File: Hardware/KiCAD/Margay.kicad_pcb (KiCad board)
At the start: 2 copper layers, 50.1 x 30.4 mm, 82 parts, among them J1 SDMMCWR-CRD, J3 CONN_6SCREW_2.54, Q1 DMG3404, Q2 FDN360P, Q3 2N7002, U1 ATMEGA1284M, U10 TLV3691DPF, U11 MIC94090C6, U12 BME280, U13 MAX6070AAUT18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

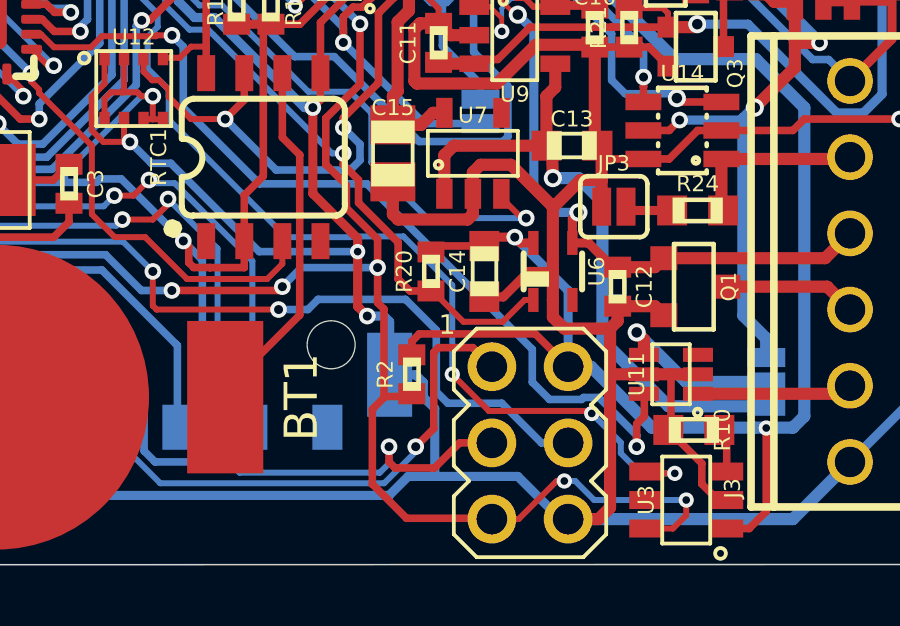
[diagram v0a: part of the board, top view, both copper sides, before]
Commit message: 3V3 --> Schottky diode --> VCoin+. Provide a backup option for the clock if its battery fails: the main batteries of the data logger. Ideally, this would have been connected to VBat to keep the coin cell as just a backup. But I cannot see how to route that trace. However, this will at least serve to protect timekeeping.
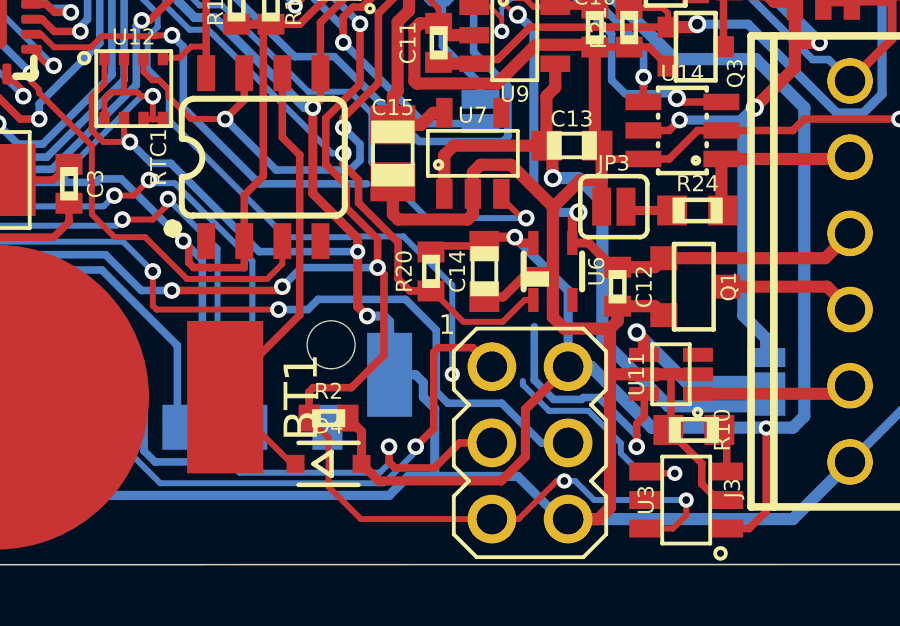
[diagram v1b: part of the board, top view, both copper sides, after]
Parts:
- added D4: BAT43WS, Margay:SOD323-R, F.Cu at (152.4, 116.8)
- H1, H2: value (none) -> MOUNTING_HOLE4_NP_CLOSE
- J2: value (none) -> CONN_102.54_SCREW
- J4: value (none) -> USB_C
- Q1: value DMG3404 -> MOSFET-NCH-DMG3404L
- Q2: value FDN360P -> MOSFET_PCH-FDN360P
- Q3: value 2N7002 -> MOSFET-NCH-2N7002PW
- U11: value MIC94090C6 -> MIC9409C6
- U13: value MAX6070AAUT18 -> MAX6070AAUT
- U14: value MCP3421A1 -> MCP342
- U6: value TPS79733 -> TPS797
- U7: value TPS7A0533DBV -> TPS7A05DBV
- U9: value TPS2104 -> TPS210
- XTAL1: value CRYSTAL8MHZ5X3.2 -> CRYSTAL5X3.2
- moved R2 3.14 mm to (152.4, 115.3), turned to 0 degrees
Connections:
- net CC1 renamed /Margay_1/CC1
- net CC2 renamed /Margay_1/CC2
- net D+ renamed /Margay_1/D+
- net D- renamed /Margay_1/D-
- net DTR renamed /Margay_1/DTR
- net RX renamed /Margay_1/RX
- net SBU1 renamed /Margay_1/SBU1
- net SBU2 renamed /Margay_1/SBU2
- net SDA_EXT renamed /Margay_2/SDA_EXT
- net SD_CD renamed /Margay_1/SD_CD
- net THERM_SENSE renamed /Margay_1/THERM_SENSE
- net TX renamed /Margay_1/TX
- net VBAT_SW renamed /Margay_3/VBAT_SW
- net VCOIN+ renamed Net-(RTC1-VBAT)
- net VDIV_AX renamed Net-(JP3-Pad2)
- net VMAIN renamed /Margay_3/VMAIN
- net XTAL1 renamed Net-(U1-XTAL1)
- net XTAL2 renamed Net-(U1-XTAL2)
- net _BLUE_RX_AUX_LED renamed Net-(D2-BLUE_CATH)
- net _BLUE_STAT_LED renamed Net-(D3-BLUE_CATH)
- net _GREEN_AUX_LED renamed Net-(D2-GREEN_CATH)
- net _GREEN_STAT_LED renamed Net-(D3-GREEN_CATH)
- net _RED_STAT_LED renamed Net-(D3-RED_CATH)
- net _RED_TX_AUX_LED renamed Net-(D2-RED_CATH)
- J1 pad 8: (no net) -> unconnected-(J1-DAT1-Pad8)
- J1 pad 9: (no net) -> unconnected-(J1-DAT2-Pad9)
- J1 pad WP: (no net) -> unconnected-(J1-WRITE_PROTECT-PadWP)
- RTC1 pad 1: (no net) -> unconnected-(RTC1-32KHZ-Pad1)
- RTC1 pad 4: (no net) -> unconnected-(RTC1-RST-Pad4)
- U1 pad 30: (no net) -> unconnected-(U1-(PCINT7/ADC7)PA7-Pad30)
- U1 pad 31: (no net) -> unconnected-(U1-(PCINT6/ADC6)PA6-Pad31)
- U1 pad 32: (no net) -> unconnected-(U1-(PCINT5/ADC5)PA5-Pad32)
- U1 pad 40: (no net) -> unconnected-(U1-(PCINT8/XCK0/T0)PB0-Pad40)
- U2 pad 15: (no net) -> unconnected-(U2-CBUS0-Pad15)
- U2 pad 16: (no net) -> unconnected-(U2-CBUS3-Pad16)
- U2 pad 19: (no net) -> unconnected-(U2-RTS#-Pad19)
- U2 pad 2: (no net) -> unconnected-(U2-RI#-Pad2)
- U2 pad 4: (no net) -> unconnected-(U2-DSR#-Pad4)
- U2 pad 5: (no net) -> unconnected-(U2-DCD#-Pad5)
- U3 pad 5: (no net) -> unconnected-(U3-WAKE-Pad5)
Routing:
- net VSWITCH_CTRL: track 30.2 -> 23.0 mm
- net 3V3: track 123.5 -> 128.6 mm
- net Net-(RTC1-VBAT): track 16.6 -> 19.8 mm
- net RST: track 81.7 -> 84.1 mm
- net WD_HOLD: track 43.3 -> 41.0 mm, vias 4 -> 3

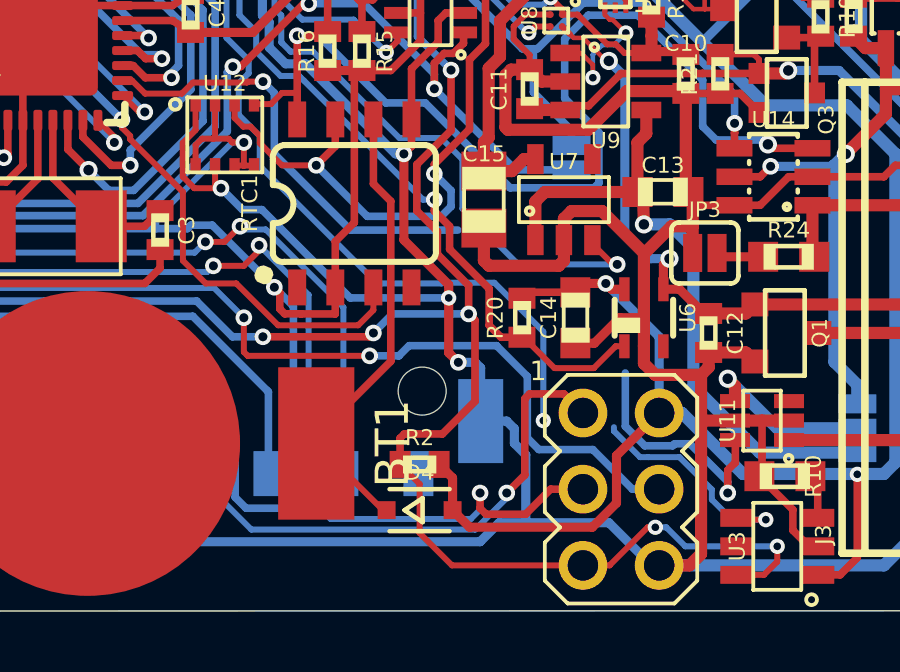
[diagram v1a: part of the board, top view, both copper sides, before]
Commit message: Add extra 1 uA decoupling cap for DS3231M. The 0.1uF cap is right by the battery, which is fine. But there was not as much buffering of power changes right by the DS3231M. And the DS3231M responds better the closer the capacitor is.
Claude Code did a quick calculation based on my finding of an up to 300 us
lag: this is the time required for a VBat handoff.
C = I × t / ΔV = 0.3 mA × 300 µs / 0.25 V = 0.36 µF

This extra capacitor might not be necessary, but considering the importance
of the RTC and the fact that we have space, I am aiming these commits to
ensure that the RTC is properly buffered from power changes and stays running.
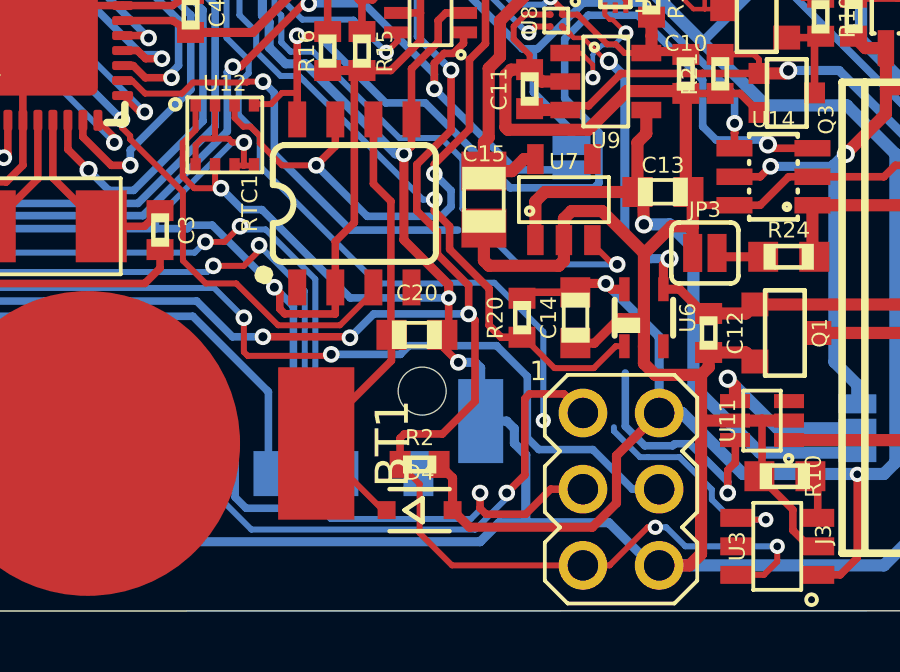
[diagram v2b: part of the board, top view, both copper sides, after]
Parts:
- added C20: 1uF, Margay:C0603, F.Cu at (152.3, 111.0)
